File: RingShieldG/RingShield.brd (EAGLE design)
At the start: 70 x 140 mm, 28 parts

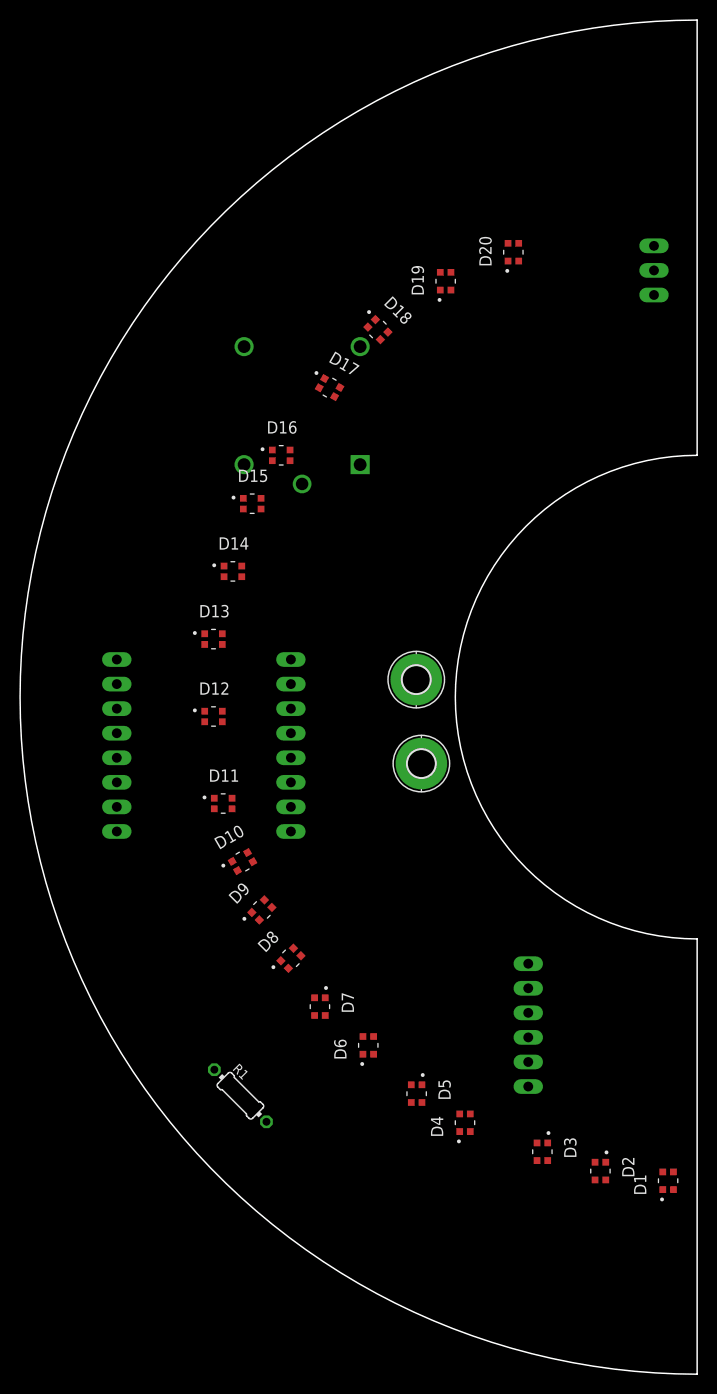
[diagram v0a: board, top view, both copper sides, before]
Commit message: Modifying the layout
Adding 2 folders for 2 pcb, as layout is limiter
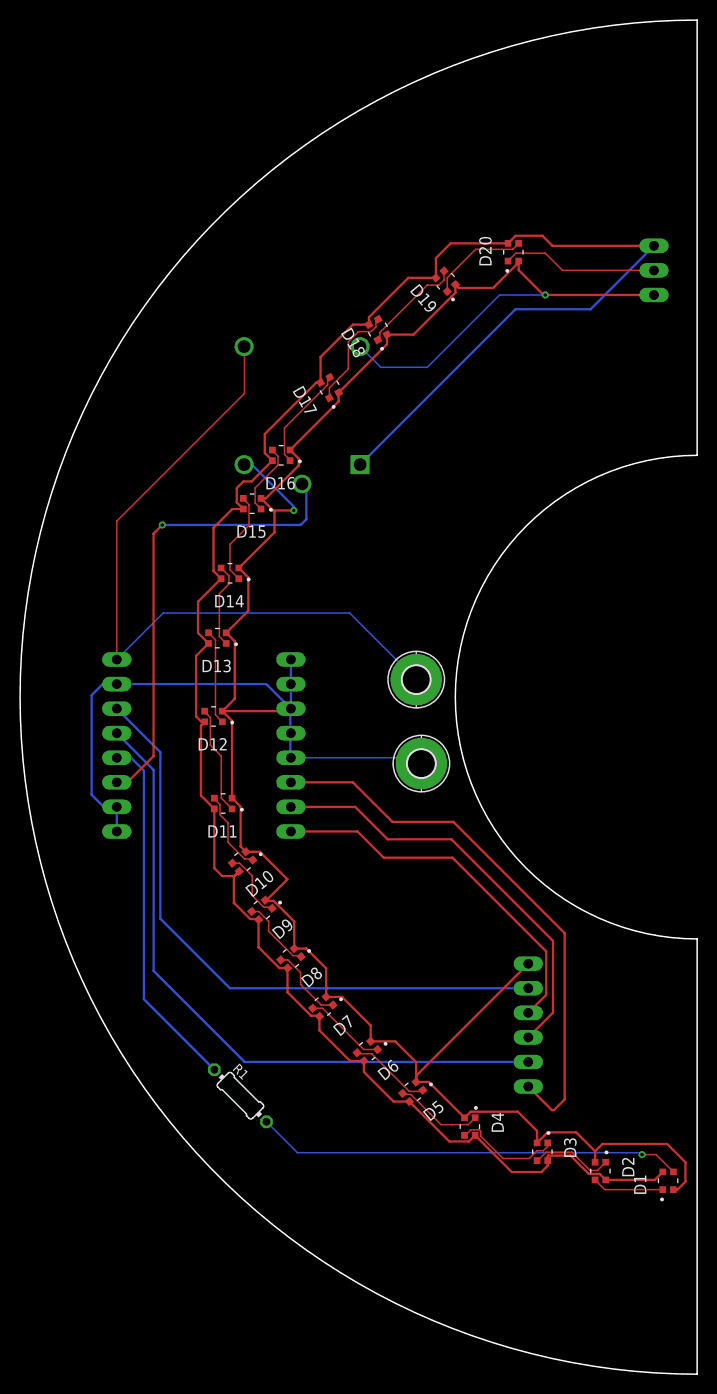
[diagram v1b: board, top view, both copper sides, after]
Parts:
- moved D4 0.64 mm to (46.5, 25.6), turned to 270 degrees
- moved D6 0.61 mm to (35.9, 33.4), turned to 220 degrees
- moved D5 0.45 mm to (40.6, 29.2), turned to 220 degrees
- moved D13 0.41 mm to (20.4, 76.1), turned to 180 degrees
- moved D14 0.36 mm to (21.7, 82.8), turned to 180 degrees
- moved D7 0.30 mm to (31.3, 38.0), turned to 220 degrees
- turned D10 to 220 degrees
- turned D11 to 180 degrees
- turned D12 to 180 degrees
- turned D15 to 180 degrees
- turned D16 to 180 degrees
- turned D17 to 120 degrees
- turned D18 to 120 degrees
- turned D19 to 130 degrees
- turned D8 to 220 degrees
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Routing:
- net GND: track 0.00 -> 294.1 mm, vias 0 -> 2
- net +5V: track 0.00 -> 215.5 mm
- net VIN: track 0.00 -> 73.6 mm
- net SCK: track 0.00 -> 68.8 mm
- net +3V3: track 0.00 -> 64.6 mm
- net CS: track 0.00 -> 57.2 mm
- net CMD: track 0.00 -> 48.2 mm, vias 0 -> 1
- net N$1: track 0.00 -> 44.2 mm, vias 0 -> 1
- net MOSI: track 0.00 -> 43.9 mm
- net MISO: track 0.00 -> 38.7 mm
- net DIN: track 0.00 -> 37.3 mm
- net DO: track 0.00 -> 16.2 mm
- net N$16: track 0.00 -> 11.3 mm
- net N$4: track 0.00 -> 11.3 mm
- net N$19: track 0.00 -> 11.0 mm
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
